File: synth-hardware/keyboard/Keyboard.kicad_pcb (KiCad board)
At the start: 2 copper layers, 295.3 x 85.7 mm, 62 parts, among them K1 SELECT, K10 F#1, K11 G1, K12 G#1, K13 A1, K14 A#1, K15 B1, K16 C2, K17 C#2, K18 D2, K19 D#2, K2 UP, K20 E2, K21 F2, K22 F#2, K23 G2, K24 G#2, K25 A2, K26 A#2, K27 B2, K28 SELECT, K29 SELECT, K3 DOWN, K30 SELECT, K31 SELECT, K32 SELECT, K4 C1, K5 C#1, K6 D1, K7 D#1, K8 E1, K9 F1, U1 RP2040

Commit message: feat(hardware): first revision pcb
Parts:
- removed K28, K29, K30, K31, K32: SELECT, KeyboardFootprints:Generic_MX_PCB_1u
- removed ST1: C_STAB, PCM_marbastlib-mx:STAB_MX_2u
- removed ST2: D_STAB, PCM_marbastlib-mx:STAB_MX_2u
- removed ST3: E_STAB, PCM_marbastlib-mx:STAB_MX_2u
- removed ST4: F_STAB, PCM_marbastlib-mx:STAB_MX_2u
- removed ST5: G_STAB, PCM_marbastlib-mx:STAB_MX_2u
- removed ST6: A_STAB, PCM_marbastlib-mx:STAB_MX_2u
- removed ST7: B_STAB, PCM_marbastlib-mx:STAB_MX_2u
- added AM2: CD74HC4067SM, Package_SO:SSOP-24_5.3x8.2mm_P0.65mm, B.Cu at (257.1, 71.5)
- added C1: 1uF, Capacitor_SMD:C_0402_1005Metric, B.Cu at (254.6, 99.0)
- added C10: 22pF, Capacitor_SMD:C_0402_1005Metric, B.Cu at (190.9, 58.2)
- added C11: 22pF, Capacitor_SMD:C_0402_1005Metric, B.Cu at (193.2, 55.4)
- added C12: 1uF, Capacitor_SMD:C_0402_1005Metric, B.Cu at (212.1, 77.2)
- added C13: 100nF, Capacitor_SMD:C_0402_1005Metric, B.Cu at (208.0, 70.9)
- added C14: 100nF, Capacitor_SMD:C_0402_1005Metric, B.Cu at (208.0, 69.7)
- added C15: 100nF, Capacitor_SMD:C_0402_1005Metric, B.Cu at (207.9, 66.8)
- added C16: 100nF, Capacitor_SMD:C_0402_1005Metric, B.Cu at (196.9, 58.1)
- added C2: 1uF, Capacitor_SMD:C_0402_1005Metric, B.Cu at (248.9, 99.8)
- added C3: 10uF, Capacitor_SMD:C_0603_1608Metric, B.Cu at (241.1, 100.1)
- added C4: 1uF, Capacitor_SMD:C_0402_1005Metric, B.Cu at (207.9, 67.8)
- added C5: 100nF, Capacitor_SMD:C_0402_1005Metric, B.Cu at (197.9, 58.1)
- added C6: 1uF, Capacitor_SMD:C_0402_1005Metric, B.Cu at (207.9, 64.2)
- added C7: 100nF, Capacitor_SMD:C_0402_1005Metric, B.Cu at (203.1, 59.3)
- added C8: 100nF, Capacitor_SMD:C_0402_1005Metric, B.Cu at (198.4, 72.9)
- added C9: 100nF, Capacitor_SMD:C_0402_1005Metric, B.Cu at (195.5, 69.3)
- added D1: Power LED (Green), LED_SMD:LED_0805_2012Metric, B.Cu at (196.4, 74.2)
- added F1: Fuse_Small, Fuse:Fuse_1206_3216Metric, B.Cu at (322.1, 64.7)
- added FID1: Fiducial, Fiducial:Fiducial_1mm_Mask2mm, F.Cu at (352.6, 55.5)
- added FID2: Fiducial, Fiducial:Fiducial_1mm_Mask2mm, F.Cu at (352.6, 59.1)
- added FID3: Fiducial, Fiducial:Fiducial_1mm_Mask2mm, F.Cu at (352.6, 62.6)
- added J1: USB_C_Receptacle_USB2.0_16P, Connector_USB:USB_C_Receptacle_HRO_TYPE-C-31-M-12, B.Cu at (326.9, 54.1)
- added J2: Conn_01x04, Connector_JST:JST_SH_SM04B-SRSS-TB_1x04-1MP_P1.00mm_Horizontal, B.Cu at (326.9, 71.0)
- added J3: Conn_01x05, Connector_PinHeader_2.54mm:PinHeader_1x05_P2.54mm_Vertical, B.Cu at (202.5, 50.2)
- added R1: 5.1k ohm, Resistor_SMD:R_0402_1005Metric, B.Cu at (325.2, 60.3)
- added R10: 1k ohm, Resistor_SMD:R_0402_1005Metric, B.Cu at (198.4, 75.3)
- added R2: 5.1k ohm, Resistor_SMD:R_0402_1005Metric, B.Cu at (329.3, 60.4)
- added R3: 5.1k ohm, Resistor_SMD:R_0402_1005Metric, B.Cu at (203.5, 57.0)
- added R4: 27 ohm, Resistor_SMD:R_0201_0603Metric, B.Cu at (210.8, 69.1)
- added R5: 27 ohm, Resistor_SMD:R_0201_0603Metric, B.Cu at (210.8, 68.1)
- added R6: 1k ohm, Resistor_SMD:R_0402_1005Metric, B.Cu at (195.9, 58.1)
- added R7: 1k ohm, Resistor_SMD:R_0402_1005Metric, B.Cu at (199.0, 100.9)
- added R8: 5.1k ohm, Resistor_SMD:R_0402_1005Metric, B.Cu at (199.0, 99.7)
- added R9: 5.1k ohm, Resistor_SMD:R_0402_1005Metric, B.Cu at (198.5, 98.0)
- added S16: C, Package_TO_SOT_SMD:SOT-23, B.Cu at (209.6, 85.7)
- added S17: C#, Package_TO_SOT_SMD:SOT-23, B.Cu at (219.1, 57.1)
- added S18: D, Package_TO_SOT_SMD:SOT-23, B.Cu at (228.6, 85.7)
- added S19: D#, Package_TO_SOT_SMD:SOT-23, B.Cu at (238.1, 57.1)
- added S20: E, Package_TO_SOT_SMD:SOT-23, B.Cu at (247.7, 85.7)
- added S21: F, Package_TO_SOT_SMD:SOT-23, B.Cu at (266.7, 85.7)
- added S22: F#, Package_TO_SOT_SMD:SOT-23, B.Cu at (276.2, 57.1)
- added S23: G, Package_TO_SOT_SMD:SOT-23, B.Cu at (285.8, 85.7)
- added S24: G#, Package_TO_SOT_SMD:SOT-23, B.Cu at (295.3, 57.1)
- added S25: A, Package_TO_SOT_SMD:SOT-23, B.Cu at (304.8, 85.7)
- added S26: A#, Package_TO_SOT_SMD:SOT-23, B.Cu at (314.3, 57.1)
- added S27: B, Package_TO_SOT_SMD:SOT-23, B.Cu at (323.9, 85.7)
- added SW1: RESET, Button_Switch_SMD:SW_SPST_TL3342, B.Cu at (207.4, 52.7)
- added SW2: BOOTSELECT, Button_Switch_SMD:SW_SPST_TL3342, B.Cu at (204.2, 99.9)
- added U2: XC6206PxxxMR, Package_TO_SOT_SMD:SOT-23-3, B.Cu at (251.8, 98.6)
- added U3: SRV05-4, PCM_marbastlib-various:SOT-23-6-routable, B.Cu at (326.9, 65.1)
- added U4: W25Q128JVS, Package_SO:SOIC-8_5.23x5.23mm_P1.27mm, B.Cu at (206.9, 75.8)
- added Y1: 12MHz 20pF, Crystal:Crystal_SMD_3225-4Pin_3.2x2.5mm, B.Cu at (193.2, 58.2)
- K1: value SELECT -> SHIFT
- moved H3 171.5 mm to (161.9, 100.0)
- moved H4 171.5 mm to (219.1, 100.0)
- moved U1 162.9 mm to (200.8, 65.4), turned to 45 degrees
- moved H5 153.1 mm to (257.2, 52.4), turned to 180 degrees
- moved H1 73.9 mm to (66.7, 100.0)
- moved H2 73.9 mm to (314.3, 100.0)
- moved H6 23.8 mm to (123.8, 52.4), turned to 180 degrees
- moved AM1 13.1 mm to (123.8, 71.5), turned to -90 degrees
- moved S15 0.33 mm to (190.5, 85.7), turned to -45 degrees
- turned K17 to 0 degrees
- turned K19 to 0 degrees
- turned K22 to 0 degrees
- turned K24 to 0 degrees
- turned K26 to 0 degrees
- turned S1 to -135 degrees
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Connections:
- net AM0:13 renamed AM1:13
- AM1 pad 1: AM0 -> AM1_COM
- AM1 pad 16: AM0:15 -> AM1:15
- AM1 pad 17: AM0:14 -> AM1:14
- AM1 pad 19: AM0:12 -> AM1:12
- AM1 pad 2: AM0:7 -> AM1:7
- AM1 pad 20: AM0:11 -> AM1:11
- AM1 pad 21: AM0:10 -> AM1:10
- AM1 pad 22: AM0:9 -> AM1:9
- AM1 pad 23: AM0:8 -> AM1:8
- AM1 pad 24: +3.3V -> +3V3
- AM1 pad 3: AM0:6 -> AM1:6
- AM1 pad 4: AM0:5 -> AM1:5
- AM1 pad 5: AM0:4 -> AM1:4
- AM1 pad 6: AM0:3 -> GND
- AM1 pad 7: AM0:2 -> AM1:2
- AM1 pad 8: AM0:1 -> AM1:1
- AM1 pad 9: AM0:0 -> AM1:0
- S1 pad 1: +3.3V -> +3V3
- S1 pad 2: AM0:7 -> AM1:6
- S10 pad 1: +3.3V -> +3V3
- S10 pad 2: AM0:10 -> AM1:2
- S11 pad 1: +3.3V -> +3V3
- S12 pad 1: +3.3V -> +3V3
- S12 pad 2: AM0:9 -> AM1:1
- S13 pad 1: +3.3V -> +3V3
- S13 pad 2: AM0:12 -> AM1:14
- S14 pad 1: +3.3V -> +3V3
- S14 pad 2: AM0:8 -> AM1:0
- S15 pad 1: +3.3V -> +3V3
- S15 pad 2: AM0:11 -> AM1:15
- S2 pad 1: +3.3V -> +3V3
- S2 pad 2: AM0:3 -> AM1:7
- S3 pad 1: +3.3V -> +3V3
- S3 pad 2: AM0:2 -> AM1:8
- S4 pad 1: +3.3V -> +3V3
- S4 pad 2: AM0:1 -> AM1:9
- S5 pad 1: +3.3V -> +3V3
- S5 pad 2: AM0:6 -> AM1:5
- S6 pad 1: +3.3V -> +3V3
- S6 pad 2: AM0:0 -> AM1:10
- S7 pad 1: +3.3V -> +3V3
- S7 pad 2: AM0:5 -> AM1:4
- S8 pad 1: +3.3V -> +3V3
- S8 pad 2: AM0:15 -> AM1:11
- S9 pad 1: +3.3V -> +3V3
- S9 pad 2: AM0:14 -> AM1:12
- U1 pad 1: Net-(U1-IOVDD-Pad1) -> +3V3
- U1 pad 10: Net-(U1-IOVDD-Pad1) -> +3V3
- U1 pad 19: unconnected-(U1-TESTEN-Pad19) -> GND
- U1 pad 2: unconnected-(U1-GPIO0-Pad2) -> USER_LED
- U1 pad 20: unconnected-(U1-XIN-Pad20) -> XIN
- U1 pad 21: unconnected-(U1-XOUT-Pad21) -> XOUT
- U1 pad 22: Net-(U1-IOVDD-Pad1) -> +3V3
- U1 pad 23: Net-(U1-DVDD-Pad23) -> +1V1
- U1 pad 24: unconnected-(U1-SWCLK-Pad24) -> SWC
- U1 pad 25: unconnected-(U1-SWD-Pad25) -> SWD
- U1 pad 26: unconnected-(U1-RUN-Pad26) -> RESET
- U1 pad 3: unconnected-(U1-GPIO1-Pad3) -> SELECT2
- U1 pad 33: Net-(U1-IOVDD-Pad1) -> +3V3
- U1 pad 34: unconnected-(U1-GPIO22-Pad34) -> SELECT6
- U1 pad 35: unconnected-(U1-GPIO23-Pad35) -> SELECT7
- U1 pad 36: unconnected-(U1-GPIO24-Pad36) -> SELECT5
- U1 pad 37: unconnected-(U1-GPIO25-Pad37) -> SELECT4
- U1 pad 38: unconnected-(U1-GPIO26_ADC0-Pad38) -> AM1_COM
- U1 pad 39: unconnected-(U1-GPIO27_ADC1-Pad39) -> AM2_COM
- U1 pad 4: unconnected-(U1-GPIO2-Pad4) -> SELECT3
- U1 pad 42: Net-(U1-IOVDD-Pad1) -> +3V3
- U1 pad 43: unconnected-(U1-ADC_AVDD-Pad43) -> +3V3
- U1 pad 44: unconnected-(U1-VREG_IN-Pad44) -> +3V3
- U1 pad 45: unconnected-(U1-VREG_VOUT-Pad45) -> +1V1
- U1 pad 46: unconnected-(U1-USB_DM-Pad46) -> Net-(U1-USB_DM)
- U1 pad 47: unconnected-(U1-USB_DP-Pad47) -> Net-(U1-USB_DP)
- U1 pad 48: unconnected-(U1-USB_VDD-Pad48) -> +3V3
- U1 pad 49: Net-(U1-IOVDD-Pad1) -> +3V3
- U1 pad 5: unconnected-(U1-GPIO3-Pad5) -> SELECT1
- U1 pad 50: Net-(U1-DVDD-Pad23) -> +1V1
- U1 pad 51: unconnected-(U1-QSPI_SD3-Pad51) -> Q_IO3
- U1 pad 52: unconnected-(U1-QSPI_SCLK-Pad52) -> Q_CLK
- U1 pad 53: unconnected-(U1-QSPI_SD0-Pad53) -> Q_IO0
- U1 pad 54: unconnected-(U1-QSPI_SD2-Pad54) -> Q_IO2
- U1 pad 55: unconnected-(U1-QSPI_SD1-Pad55) -> Q_IO1
- U1 pad 56: unconnected-(U1-QSPI_SS-Pad56) -> Q_SEL
- U1 pad 57: unconnected-(U1-GND-Pad57) -> GND
- U1 pad 6: unconnected-(U1-GPIO4-Pad6) -> SELECT0
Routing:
- net GND: track 0.00 -> 962.5 mm, vias 0 -> 60
- net +3V3: track 0.00 -> 938.9 mm, vias 0 -> 32
- net D+: track 0.00 -> 214.3 mm
- net D-: track 0.00 -> 212.5 mm
- net +5V: track 0.00 -> 113.9 mm
- net AM1_COM: track 0.00 -> 93.5 mm, vias 0 -> 2
- net SELECT0: track 0.00 -> 77.6 mm
- net SELECT2: track 0.00 -> 77.2 mm
- net SELECT1: track 0.00 -> 77.2 mm
- net AM1:8: track 0.00 -> 76.1 mm
- net SELECT3: track 0.00 -> 75.2 mm
- net AM1:15: track 0.00 -> 70.0 mm
- net AM2:7: track 0.00 -> 68.3 mm
- net AM1:6: track 0.00 -> 68.2 mm
- net AM1:7: track 0.00 -> 67.9 mm
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- added copper zone on B.Cu, net GND
- added copper zone on F.Cu, net GND
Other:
- board size 295.3 x 85.7 mm -> 284.2 x 55.6 mm

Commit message: feat(hardware): fix usb and add more components
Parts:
- removed R3: 5.1k ohm, Resistor_SMD:R_0402_1005Metric
- removed SW1: RESET, Button_Switch_SMD:SW_SPST_TL3342
- FID1, FID2, FID3: moved to B.Cu
- R4, R5: footprint Resistor_SMD:R_0201_0603Metric -> Resistor_SMD:R_0603_1608Metric
- S1, S10, S11, S12, S13, S14, S15, S16, S17, S18, S19, S2, S20, S21, S22, S23, S24, S25, S26, S27, S3, S4, S5, S6, S7, S8, S9: footprint Package_TO_SOT_SMD:SOT-23 -> Package_TO_SOT_SMD:SOT-23-3
- moved FID1 278.9 mm to (92.9, 157.2), turned to 180 degrees
- moved H2 233.3 mm to (88.1, 157.2)
- moved H6 231.0 mm to (347.7, 109.5)
- moved H3 194.3 mm to (347.7, 157.2)
- moved H5 109.3 mm to (226.2, 157.2)
- moved FID2 93.2 mm to (347.7, 152.2), turned to 180 degrees
- moved R1 72.7 mm to (278.5, 116.1)
- moved J1 72.7 mm to (280.3, 109.8)
- moved R2 72.7 mm to (282.6, 116.1)
- moved U3 71.5 mm to (280.3, 119.3)
- moved F1 70.4 mm to (275.7, 117.6)
- moved J2 67.8 mm to (270.7, 109.0), turned to 0 degrees
- moved C7 61.7 mm to (221.9, 118.1), turned to 135 degrees
- moved R4 60.6 mm to (230.7, 126.3)
- moved R10 60.2 mm to (217.4, 132.5)
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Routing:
- net +3V3: track 938.9 -> 794.8 mm, vias 32 -> 39
- net D-: track 212.5 -> 73.3 mm, vias 0 -> 3
- net D+: track 214.3 -> 76.8 mm, vias 0 -> 3
- net +5V: track 113.9 -> 33.7 mm, vias 0 -> 2
- net GND: track 962.5 -> 917.7 mm, vias 60 -> 58
- net +1V1: track 39.5 -> 51.6 mm
- net RESET: track 22.8 -> 13.0 mm
- net VBUS: track 14.1 -> 11.5 mm
- net AM2:4: track 14.1 -> 13.1 mm
- net Net-(U1-USB_DP): track 7.38 -> 8.17 mm
- net Net-(U1-USB_DM): track 7.06 -> 7.62 mm

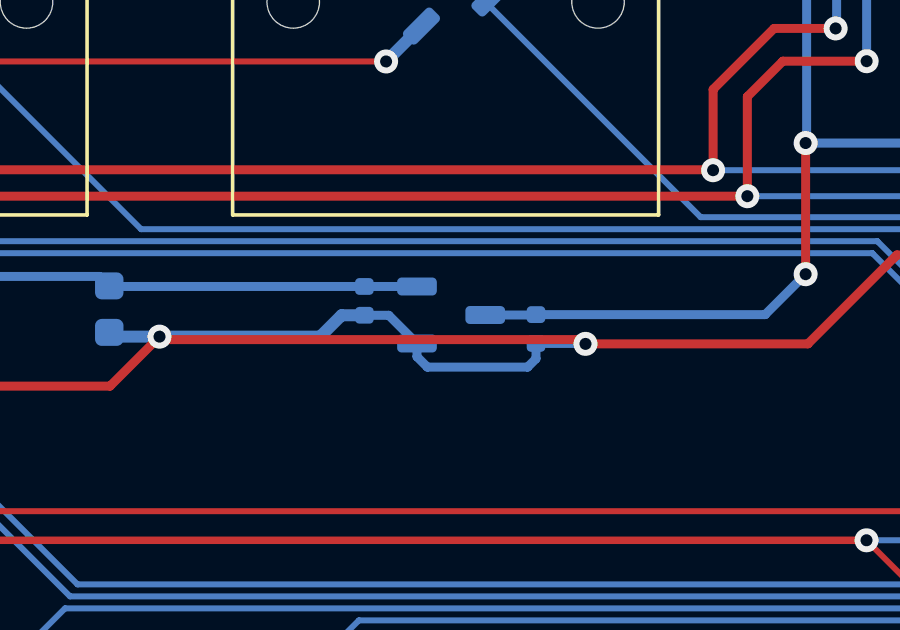
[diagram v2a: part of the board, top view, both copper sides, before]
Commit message: feat(hardware): finished adding lcsc for all components
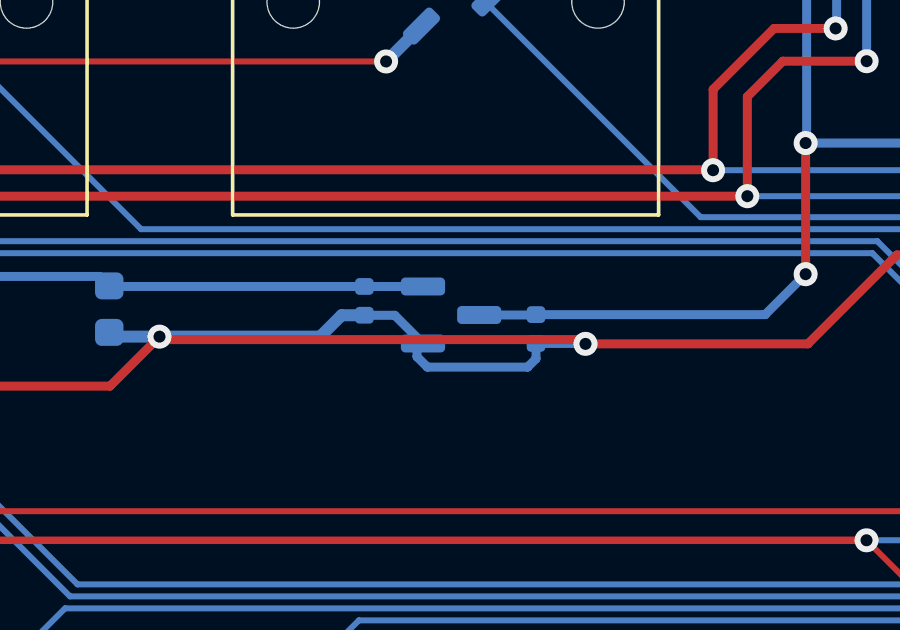
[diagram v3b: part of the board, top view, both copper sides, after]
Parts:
- F1: value Fuse_Small -> 6V 1.5A
- U2: value XC6206PxxxMR -> XC6206P332MR; footprint Package_TO_SOT_SMD:SOT-23-3 -> Package_TO_SOT_SMD:SOT-23
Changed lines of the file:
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@@
 		)
 	)
-	(footprint "Package_TO_SOT_SMD:SOT-23-3"
+	(footprint "Package_TO_SOT_SMD:SOT-23"
 		(layer "B.Cu")
 		(at 257.357611 124.735358)
-		(descr "SOT, 3 Pin (https://www.jedec.org/sites/default/files/docs/Mo-178D.PDF inferred 3-pin variant), generated with kicad-footprint-generator ipc_gullwing_generator.py")
+		(descr "SOT, 3 Pin (https://www.jedec.org/system/files/docs/to-236h.pdf variant AB), generated with kicad-footprint-generator ipc_gullwing_generator.py")
 		(tags "SOT TO_SOT_SMD")
 		(property "Reference" "U2"
-			(at 0.077712 2.734749 180)
+			(at 0.010612 2.718049 180)
 			(layer "B.SilkS")
 			(effects
@@
 			)
 		)
-		(property "Value" "XC6206PxxxMR"
+		(property "Value" "XC6206P332MR"
 			(at 0 -2.4 180)
 			(layer "B.Fab")
@@
 			)
 		)
-		(property "Footprint" "Package_TO_SOT_SMD:SOT-23-3"
+		(property "Footprint" "Package_TO_SOT_SMD:SOT-23"
 			(at 0 0 180)
+			(unlocked yes)
 			(layer "B.Fab")
 			(hide yes)
@@
 		(property "Datasheet" "https://www.torexsemi.com/file/xc6206/XC6206.pdf"
 			(at 0 0 180)
+			(unlocked yes)
 			(layer "B.Fab")
 			(hide yes)
@@
 		(property "Description" ""
 			(at 0 0 180)
+			(unlocked yes)
 			(layer "B.Fab")
 			(hide yes)
@@
 			)
 		)
-		(property "LCSC" "??"
+		(property "LCSC" "C5148692"
 			(at 0 0 0)
 			(unlocked yes)
@@
 		(attr smd)
 		(fp_line
-			(start -0.8 -1.56)
+			(start -0.65 -1.56)
 			(end 0 -1.56)
 			(stroke
@@
 		)
 		(fp_line
-			(start -0.8 1.56)
+			(start -0.65 1.56)
 			(end 0 1.56)
 			(stroke
@@
 		)
 		(fp_line
-			(start 0.8 -1.56)
+			(start 0.65 -1.56)
 			(end 0 -1.56)
 			(stroke
@@
 		)
 		(fp_line
-			(start 0.8 1.56)
+			(start 0.65 1.56)
 			(end 0 1.56)
 			(stroke
@@
 		(fp_poly
 			(pts
-				(xy -1.3 1.51) (xy -1.54 1.84) (xy -1.06 1.84) (xy -1.3 1.51)
+				(xy -1.1625 1.51) (xy -1.4025 1.84) (xy -0.9225 1.84) (xy -1.1625 1.51)
 			)
 			(stroke
@@
 		)
 		(fp_line
-			(start -2.05 -1.7)
-			(end -2.05 1.7)
+			(start -1.92 -1.7)
+			(end -1.92 1.7)
 			(stroke
 				(width 0.05)
@@
 		)
 		(fp_line
-			(start -2.05 1.7)
-			(end 2.05 1.7)
+			(start -1.92 1.7)
+			(end 1.92 1.7)
 			(stroke
 				(width 0.05)
@@
 		)
 		(fp_line
-			(start 2.05 -1.7)
-			(end -2.05 -1.7)
+			(start 1.92 -1.7)
+			(end -1.92 -1.7)
 			(stroke
 				(width 0.05)
@@
 		)
 		(fp_line
-			(start 2.05 1.7)
-			(end 2.05 -1.7)
+			(start 1.92 1.7)
+			(end 1.92 -1.7)
 			(stroke
 				(width 0.05)
@@
 		)
 		(fp_line
-			(start -0.8 -1.45)
-			(end 0.8 -1.45)
+			(start -0.65 -1.45)
+			(end 0.65 -1.45)
 			(stroke
 				(width 0.1)
@@
 		)
 		(fp_line
-			(start -0.8 1.05)
-			(end -0.8 -1.45)
+			(start -0.65 1.125)
+			(end -0.65 -1.45)
 			(stroke
 				(width 0.1)
@@
 		)
 		(fp_line
-			(start -0.4 1.45)
-			(end -0.8 1.05)
+			(start -0.325 1.45)
+			(end -0.65 1.125)
 			(stroke
 				(width 0.1)
@@
 		)
 		(fp_line
-			(start 0.8 -1.45)
-			(end 0.8 1.45)
+			(start 0.65 -1.45)
+			(end 0.65 1.45)
 			(stroke
 				(width 0.1)
@@
 		)
 		(fp_line
-			(start 0.8 1.45)
-			(end -0.4 1.45)
+			(start 0.65 1.45)
+			(end -0.325 1.45)
 			(stroke
 				(width 0.1)
@@
 			(effects
 				(font
-					(size 0.4 0.4)
-					(thickness 0.06)
+					(size 0.32 0.32)
+					(thickness 0.05)
 				)
 				(justify mirror)
@@
 		)
 		(pad "1" smd roundrect
-			(at -1.1375 0.95)
-			(size 1.325 0.6)
+			(at -0.9375 0.95)
+			(size 1.475 0.6)
 			(layers "B.Cu" "B.Paste" "B.Mask")
 			(roundrect_rratio 0.25)
@@
 		)
 		(pad "2" smd roundrect
-			(at -1.1375 -0.95)
-			(size 1.325 0.6)
+			(at -0.9375 -0.95)
+			(size 1.475 0.6)
 			(layers "B.Cu" "B.Paste" "B.Mask")
 			(roundrect_rratio 0.25)
@@
 		)
 		(pad "3" smd roundrect
-			(at 1.1375 0)
-			(size 1.325 0.6)
+			(at 0.9375 0)
+			(size 1.475 0.6)
 			(layers "B.Cu" "B.Paste" "B.Mask")
 			(roundrect_rratio 0.25)
@@
 			(pintype "power_in")
 		)
-		(model "${KICAD8_3DMODEL_DIR}/Package_TO_SOT_SMD.3dshapes/SOT-23-3.wrl"
+		(model "${KICAD8_3DMODEL_DIR}/Package_TO_SOT_SMD.3dshapes/SOT-23.wrl"
 			(offset
 				(xyz 0 0 0)
@@
 			)
 		)
-		(property "Value" "Fuse_Small"
+		(property "Value" "6V 1.5A"
 			(at 0 -1.82 90)
 			(layer "B.Fab")
@@
 			)
 		)
-		(property "LCSC" "??"
+		(property "LCSC" "C2838983"
 			(at 0 0 -90)
 			(unlocked yes)
@@
 	)
 	(segment
+		(start 255.479565 124.744812)
+		(end 256.420111 125.685358)
+		(width 0.3)
+		(layer "B.Cu")
+		(net 7)
+	)
+	(segment
 		(start 215.979192 114.364053)
 		(end 215.979192 114.825)
@@
 	)
 	(segment
-		(start 255.279565 124.744812)
-		(end 256.220111 125.685358)
-		(width 0.3)
-		(layer "B.Cu")
-		(net 7)
-	)
-	(segment
 		(start 146.41 125.045)
 		(end 146.41 128.19)
@@
 	)
 	(segment
+		(start 254.466789 124.744812)
+		(end 255.479565 124.744812)
+		(width 0.3)
+		(layer "B.Cu")
+		(net 7)
+	)
+	(segment
 		(start 272.61 129)
 		(end 272.61 132.245)
@@
 	)
 	(segment
-		(start 254.466789 124.744812)
-		(end 255.279565 124.744812)
-		(width 0.3)
-		(layer "B.Cu")
-		(net 7)
-	)
-	(segment
 		(start 227.475 121.365)
 		(end 228.605 121.365)
@@
 	)
 	(segment
+		(start 254.467335 123.785358)
+		(end 254.466789 123.784812)
+		(width 0.3)
+		(layer "B.Cu")
+		(net 10)
+	)
+	(segment
 		(start 223.811459 123.415925)
 		(end 224.380534 123.985)
@@
 	)
 	(segment
+		(start 256.420111 123.785358)
+		(end 254.467335 123.785358)
+		(width 0.3)
+		(layer "B.Cu")
+		(net 10)
+	)
+	(segment
 		(start 104.766161 112.965336)
 		(end 104.821428 112.965336)
@@
 	)
 	(segment
-		(start 254.466789 123.784812)
-		(end 256.219565 123.784812)
-		(width 0.3)
-		(layer "B.Cu")
-		(net 10)
-	)
-	(segment
 		(start 219.232943 126.810037)
 		(end 218.540121 127.502859)
@@
 	)
 	(segment
-		(start 258.495111 124.735358)
-		(end 260.174921 124.735358)
-		(width 0.3)
-		(layer "B.Cu")
-		(net 11)
-	)
-	(segment
 		(start 275.675 119.003604)
 		(end 275.925 119.253604)
@@
 		(width 0.3)
 		(layer "B.Cu")
+		(net 11)
+	)
+	(segment
+		(start 258.295111 124.735358)
+		(end 260.174921 124.735358)
+		(width 0.3)
+		(layer "B.Cu")

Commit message: feat: dump of hardware changes and firmware
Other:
- board text added: "Paul Lavender-Jones"
- board text added: "REV A 11/24"
